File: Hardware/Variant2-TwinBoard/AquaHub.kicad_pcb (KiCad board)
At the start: 2 copper layers, 184 x 119 mm, 87 parts, among them J1 Screw_Terminal_01x02, J10 PinHeader6, J11 Power_Conn, J13 PinHeader2, J14 PinHeader3, J2 Screw_Terminal_01x02, J3 Screw_Terminal_01x02, J4 Screw_Terminal_01x02, J5 Screw_Terminal_01x02, J6 Screw_Terminal_01x02, J7 Control_Conn, J8 Screw_Terminal_01x02, J9 PinHeader3, K1 5A Relay, K2 5A Relay, K3 5A Relay, K4 5A Relay, K5 5A Relay, K6 5A Relay, Q1 BSS138, Q2 2SC1815, SW1 SW_Push, SW2 SW_Push, SW3 SW_Push, SW4 SW_Push, SW5 SW_Push, SW6 SW_Push, U1 ESP32-WROOM, U2 Current Sense, U3 1A 3.3V, U4 Low-Side Driver, U5 1A 5V, U6 TCA9534, U7 DS1307+, Y1 32.768KHz

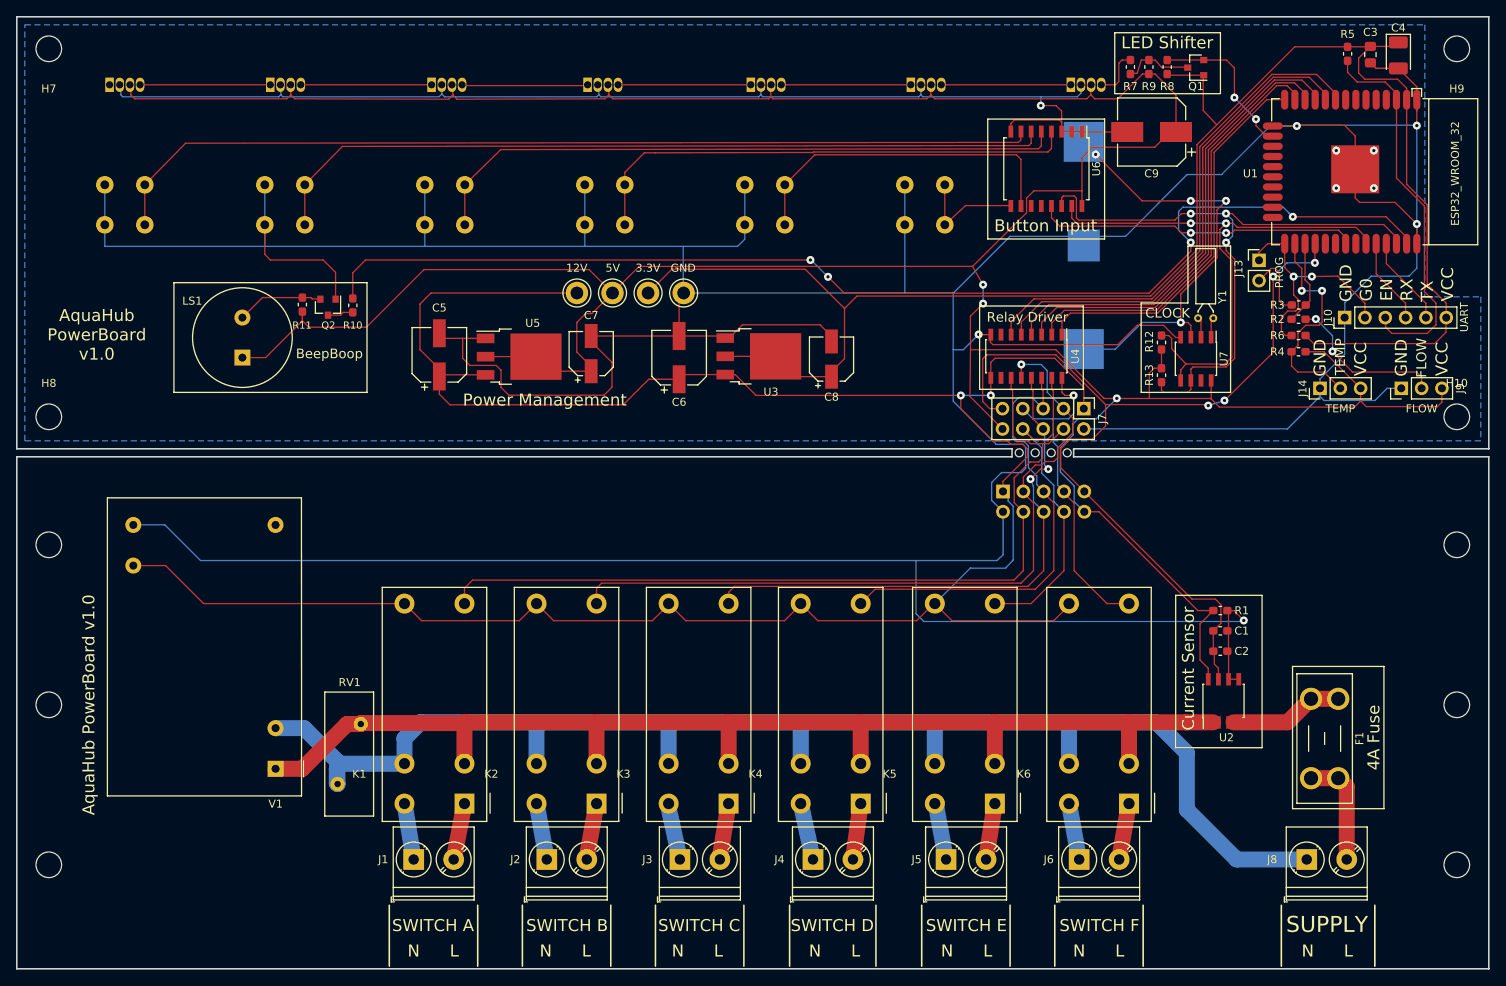
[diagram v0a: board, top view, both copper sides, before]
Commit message: New TwinBoard layout
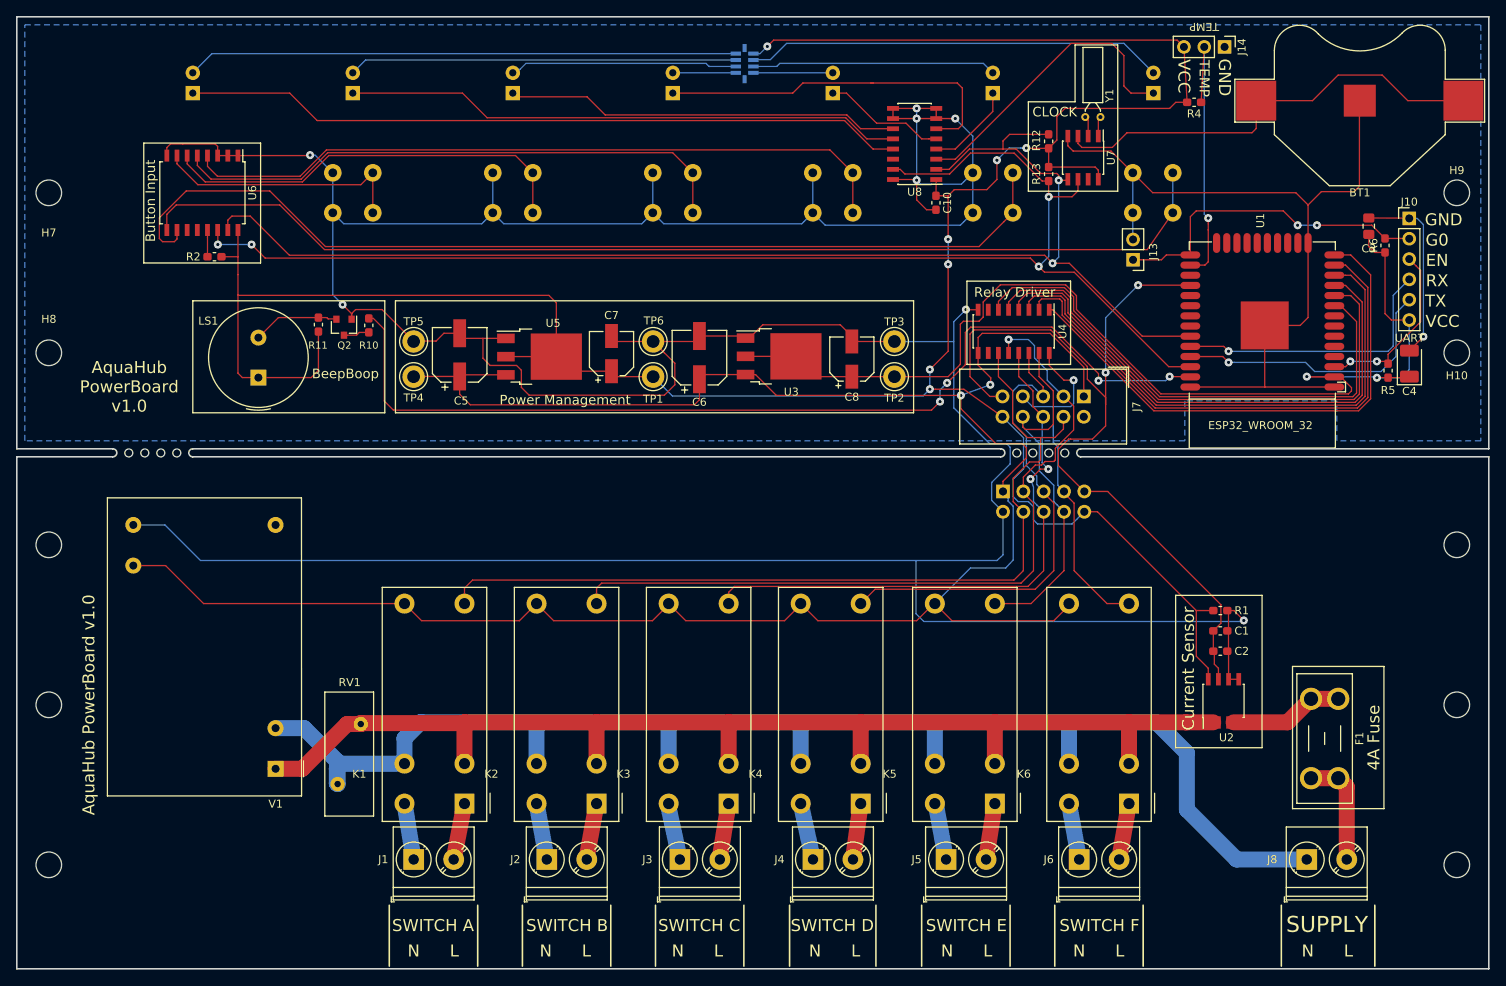
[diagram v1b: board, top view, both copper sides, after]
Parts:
- removed C9: 220uF, Capacitor_SMD:CP_Elec_8x6.2
- removed J9: PinHeader3, Connector_PinHeader_2.54mm:PinHeader_1x03_P2.54mm_Vertical
- removed Q1: BSS138, Package_TO_SOT_SMD:SOT-23
- removed R3: 3.3K, Resistor_SMD:R_0603_1608Metric_Pad1.05x0.95mm_HandSolder
- removed R7: 500R, Resistor_SMD:R_0603_1608Metric_Pad1.05x0.95mm_HandSolder
- removed R8, R9: 10k, Resistor_SMD:R_0603_1608Metric_Pad1.05x0.95mm_HandSolder
- removed REF** (x4): Breakaway 1mm, AquaFootprints:Breakaway 1mm
- added C10: 100nF, Capacitor_SMD:C_0603_1608Metric_Pad1.05x0.95mm_HandSolder, F.Cu at (167.9, 56.2)
- added H11: MountingHole, AquaFootprints:Breakaway 1mm, F.Cu at (178.0, 87.5)
- added H12: MountingHole, AquaFootprints:Breakaway 1mm, F.Cu at (67.0, 87.5)
- added H13: MountingHole, AquaFootprints:Breakaway 1mm, F.Cu at (180.0, 87.5)
- added H14: MountingHole, AquaFootprints:Breakaway 1mm, F.Cu at (69.0, 87.5)
- added H15: MountingHole, AquaFootprints:Breakaway 1mm, F.Cu at (182.0, 87.5)
- added H16: MountingHole, AquaFootprints:Breakaway 1mm, F.Cu at (71.0, 87.5)
- added H17: MountingHole, AquaFootprints:Breakaway 1mm, F.Cu at (184.0, 87.5)
- added H18: MountingHole, AquaFootprints:Breakaway 1mm, F.Cu at (73.0, 87.5)
- added RN1: R_Network08, AquaFootprints:CAT25, B.Cu at (145.0, 37.6)
- added TP5: Test_12V_GND, TestPoint:TestPoint_Keystone_5010-5014_Multipurpose, F.Cu at (102.6, 73.6)
- added TP6: TEST_5V_GND, TestPoint:TestPoint_Keystone_5010-5014_Multipurpose, F.Cu at (132.5, 73.6)
- added U8: TPIC2810D, Package_SO:SOIC-16_3.9x9.9mm_P1.27mm, F.Cu at (165.2, 48.9)
- BT1: moved to F.Cu
- D1, D2, D3, D4, D5, D6, D7: value WS2811 -> LED; footprint LED_THT:LED_D5.0mm-4_RGB -> LED_THT:LED_D5.0mm
- J7: footprint Connector_PinHeader_2.54mm:PinHeader_2x05_P2.54mm_Vertical -> Connector_IDC:IDC-Header_2x05_P2.54mm_Vertical
- R12, R13, R4: value 4.7K -> 4.7k
- R2: value 2.2K -> 4.7k
- TP1: value TestPoint -> TEST_5V
- TP2: value TestPoint -> Test_3V3
- TP3: value TestPoint -> Test_3V3_GND
- TP4: value TestPoint -> Test_12V
- moved R2 135.7 mm to (77.7, 63.0), turned to 180 degrees
- moved D7 109.8 mm to (75.0, 42.5), turned to 90 degrees
- moved U6 105.5 mm to (76.2, 55.0)
- moved J14 44.3 mm to (204.0, 36.8), turned to 270 degrees
- moved R5 39.9 mm to (224.4, 77.2), turned to 90 degrees
- moved C4 38.6 mm to (227.1, 76.4), turned to 90 degrees
- moved BT1 37.8 mm to (207.9, 43.5), turned to 0 degrees
- moved R4 33.8 mm to (200.2, 43.7), turned to 180 degrees
- moved TP2 32.5 mm to (162.7, 78.0), turned to 0 degrees
- moved D3 30.7 mm to (155.0, 42.5), turned to 90 degrees
- moved D6 30.4 mm to (95.0, 42.5), turned to 90 degrees
- moved D1 30.3 mm to (195.1, 42.5), turned to 90 degrees
- moved D5 30.3 mm to (115.0, 42.5), turned to 90 degrees
- moved D2 30.3 mm to (175.0, 42.5), turned to 90 degrees
- moved D4 30.2 mm to (135.0, 42.5), turned to 90 degrees
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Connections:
- net /Panel_SCL renamed SCL
- net /Panel_SDA renamed SDA
- net /Power_Sense renamed Power_Sense
- net /RE1 renamed RE1
- net /RE2 renamed RE2
- net /RE3 renamed RE3
- net /RE4 renamed RE4
- net /RE5 renamed RE5
- net /RE6 renamed RE6
- BT1 pad 1: +3V3 -> +BATT
- D1 pad 2: GND -> Net-(D1-Pad2)
- D2 pad 2: GND -> Net-(D2-Pad2)
- D3 pad 2: GND -> Net-(D3-Pad2)
- D4 pad 2: GND -> Net-(D4-Pad2)
- D5 pad 2: GND -> Net-(D5-Pad2)
- D6 pad 2: GND -> Net-(D6-Pad2)
- D7 pad 1: Net-(D1-Pad4) -> Net-(D7-Pad1)
- D7 pad 2: GND -> Net-(D7-Pad2)
- R2 pad 1: /Flow_Sense -> +5V
- R2 pad 2: Net-(J9-Pad2) -> Net-(R2-Pad2)
- U1 pad 16: /Panel_LED_33 -> (no net)
- U1 pad 17: Net-(U1-Pad17) -> (no net)
- U1 pad 18: Net-(U1-Pad18) -> (no net)
- U1 pad 19: Net-(U1-Pad19) -> (no net)
- U1 pad 20: Net-(U1-Pad20) -> (no net)
- U1 pad 21: Net-(U1-Pad21) -> (no net)
- U1 pad 22: Net-(U1-Pad22) -> (no net)
- U1 pad 23: Net-(U1-Pad23) -> (no net)
- U1 pad 24: Net-(U1-Pad24) -> (no net)
- U1 pad 27: /Flow_Sense -> (no net)
- U1 pad 29: Net-(U1-Pad29) -> (no net)
- U1 pad 30: Net-(U1-Pad30) -> (no net)
- U1 pad 31: /Panel_INT -> (no net)
- U1 pad 32: Net-(U1-Pad32) -> (no net)
- U1 pad 4: Net-(U1-Pad4) -> (no net)
- U1 pad 5: Net-(U1-Pad5) -> (no net)
- U1 pad 6: Net-(U1-Pad6) -> (no net)
- U1 pad 7: Net-(U1-Pad7) -> (no net)
- U1 pad 8: Net-(U1-Pad8) -> (no net)
- U4 pad 10: Net-(U4-Pad10) -> (no net)
- U4 pad 7: Net-(U4-Pad7) -> (no net)
- U6 pad 11: Net-(U6-Pad11) -> (no net)
- U6 pad 12: Net-(U6-Pad12) -> (no net)
- U6 pad 13: /Panel_INT -> Net-(R2-Pad2)
- U7 pad 3: +3V3 -> +BATT
- U7 pad 7: Net-(U7-Pad7) -> (no net)
- V1 pad 3: Net-(V1-Pad3) -> (no net)
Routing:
- net GND: track 867.2 -> 640.8 mm, vias 10 -> 9
- net +5V: track 474.1 -> 341.2 mm, vias 3 -> 7
- net +3V3: track 270.9 -> 138.2 mm, vias 4 -> 2
- net Net-(SW1-Pad1): track 14.1 -> 137.9 mm
- net SDA: track 71.4 -> 165.4 mm
- net Net-(D7-Pad1): track 0.00 -> 90.4 mm
- net SCL: track 80.9 -> 168.5 mm, vias 3 -> 4
- net Net-(SW6-Pad1): track 117.9 -> 32.2 mm
- net Net-(SW2-Pad1): track 42.1 -> 123.9 mm
- net Net-(D6-Pad1): track 0.00 -> 69.9 mm
- net Net-(D7-Pad2): track 0.00 -> 68.9 mm
- net +BATT: track 0.00 -> 56.4 mm
- net Net-(D1-Pad2): track 0.00 -> 52.4 mm
- net Net-(D6-Pad2): track 0.00 -> 48.5 mm
- net Net-(SW5-Pad1): track 99.8 -> 52.4 mm
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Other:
- outline, holes or cut-outs redrawn
- board text removed: "12V"
- board text removed: "3.3V"
- board text removed: "5V"
- board text removed: "FLOW"
- board text removed: "LED Shifter"
- board text removed: "PROG"
